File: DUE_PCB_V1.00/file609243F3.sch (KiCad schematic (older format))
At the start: 24 parts, among them J26 Motor_Left2, J37 RPM_Mow, J38 ODO_Left, J39 ODO_Right, J40 Motor_Right, J41 Motor_Left, J42 Cutter, J7 Motor_Right2, U1 MC33926, U2 MC33926

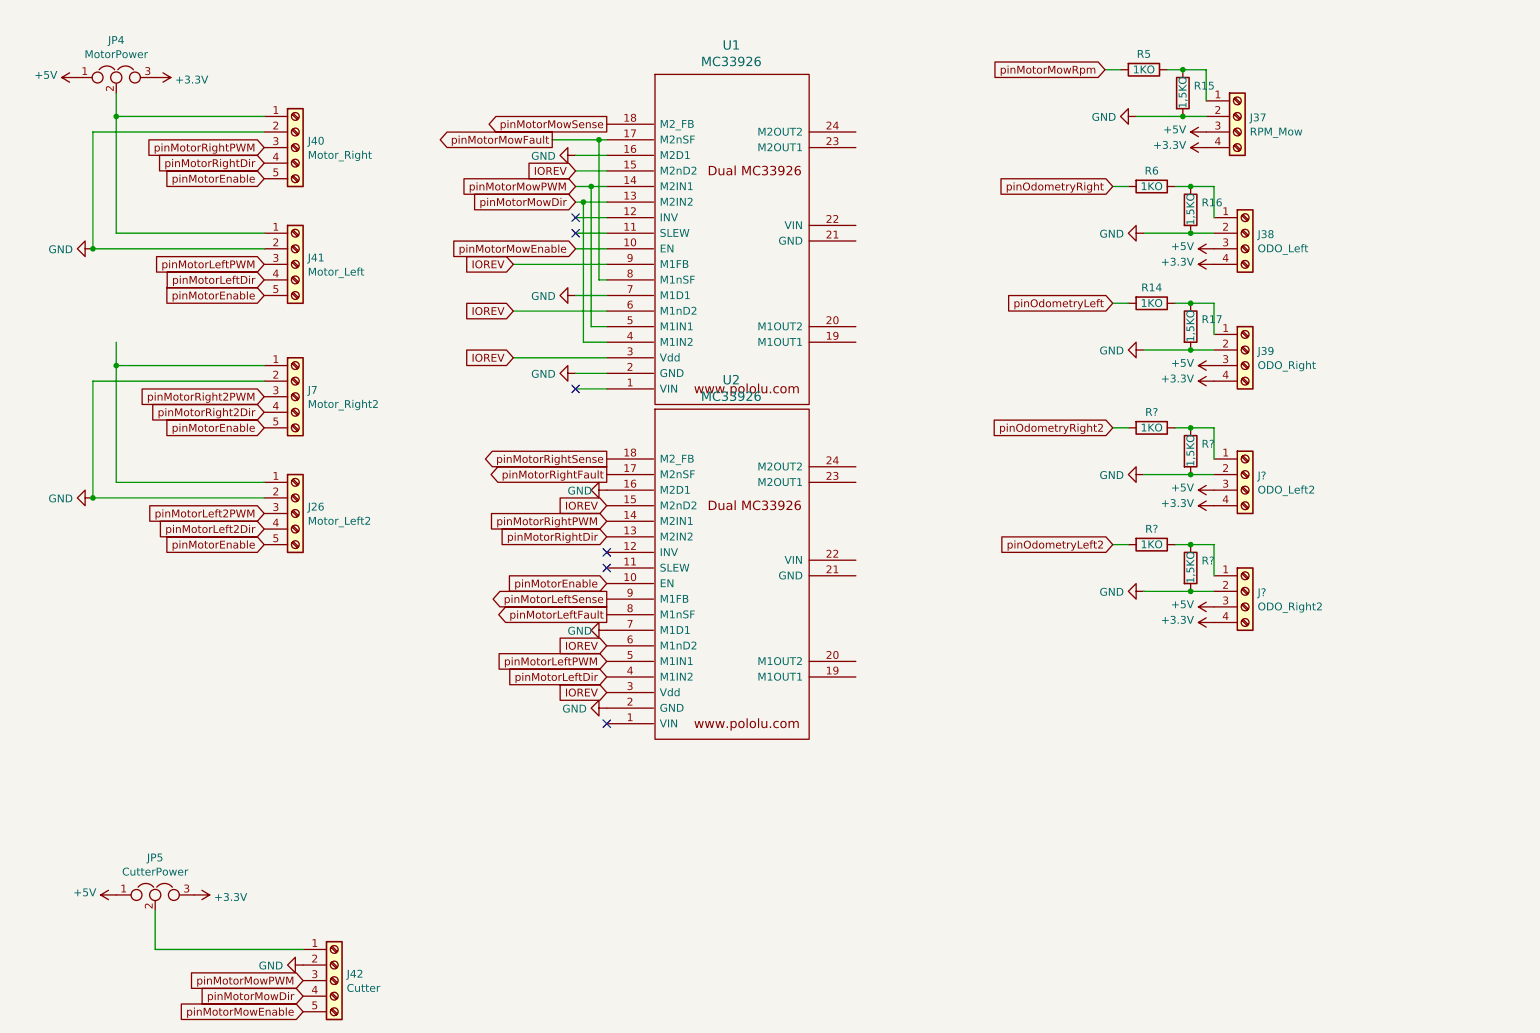
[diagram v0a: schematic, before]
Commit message: New Pins added
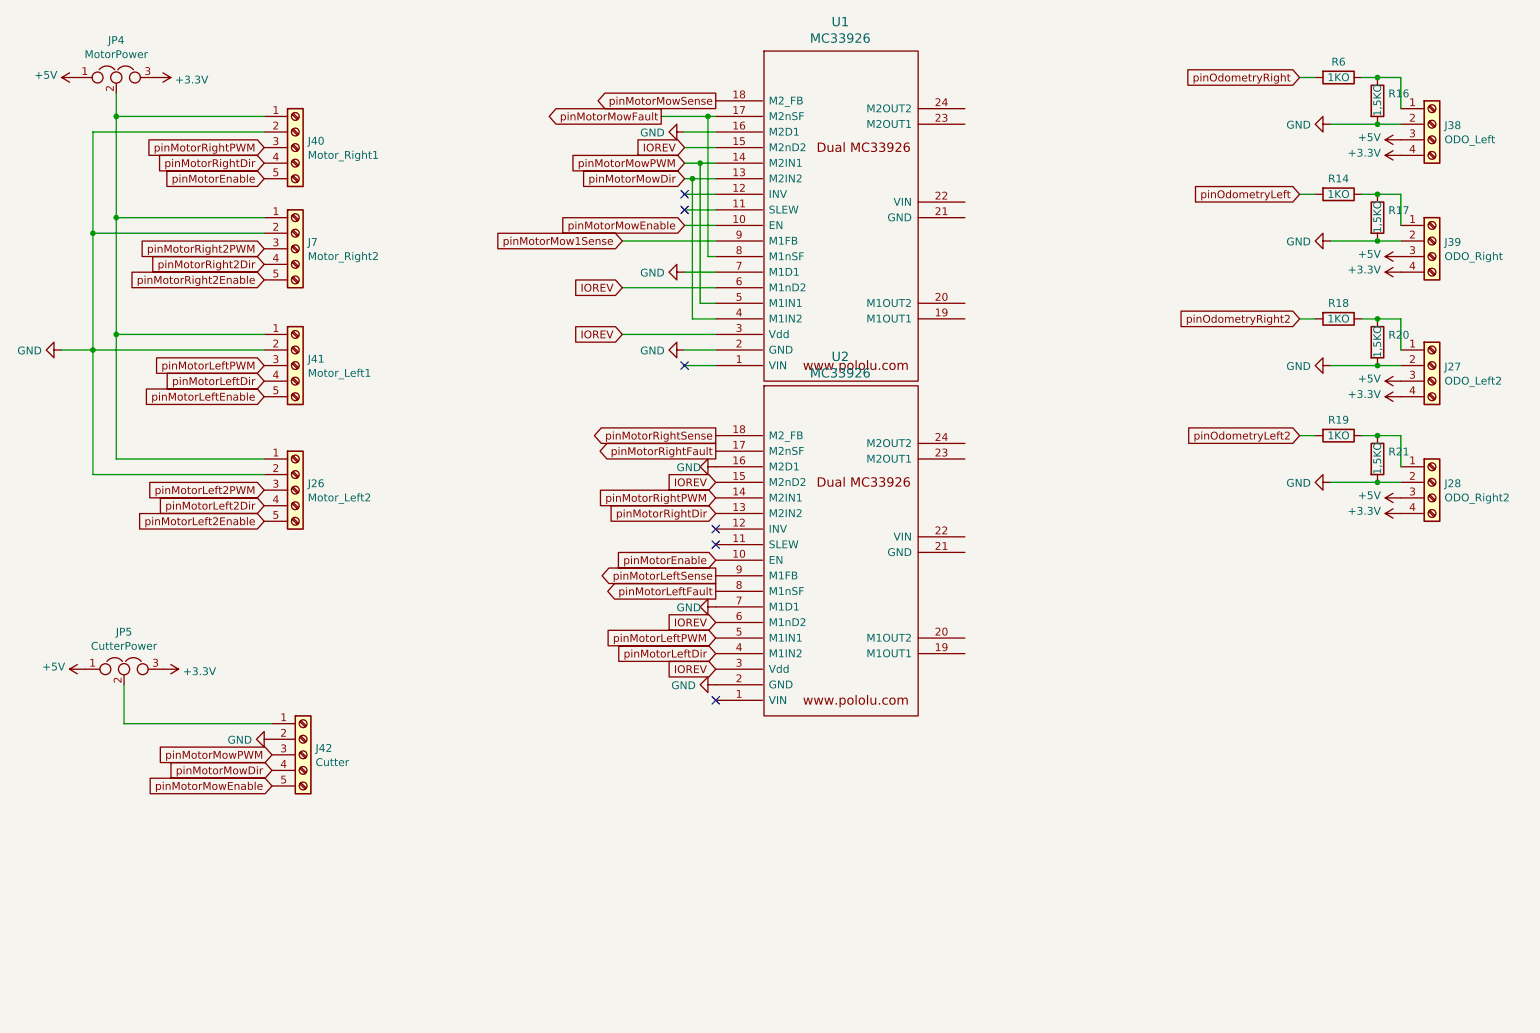
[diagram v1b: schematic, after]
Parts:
- removed J37: RPM_Mow, Connector_PinHeader_2.54mm:PinHeader_1x04_P2.54mm_Vertical, symbol Connector:Screw_Terminal_01x04
- removed R15: 1,5KO, Resistor_THT:R_Axial_DIN0207_L6.3mm_D2.5mm_P2.54mm_Vertical, symbol Device:R
- removed R5: 1KO, Resistor_THT:R_Axial_DIN0207_L6.3mm_D2.5mm_P2.54mm_Vertical, symbol Device:R
- J40: value Motor_Right -> Motor_Right1
- J41: value Motor_Left -> Motor_Left1
- gave numbers to parts that had none: 6
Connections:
- net IOREV: no longer U1.9 (M1FB)
- net pinMotorEnable: no longer J26.5 (Pin_5), J41.5 (Pin_5), J7.5 (Pin_5)
- net at J40.1 (Pin_1), J41.1 (Pin_1), JP4.2: now also J26.1 (Pin_1), J7.1 (Pin_1)
- new net pinMotorLeft2Enable: J26.5 (Pin_5)
- new net pinMotorLeftEnable: J41.5 (Pin_5)
- new net pinMotorMow1Sense: U1.9 (M1FB)
- new net pinMotorRight2Enable: J7.5 (Pin_5)
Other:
- moved on the sheet: J26, J27, J28, J38, J39, J41, J42, J7, JP5, R14, R16, R17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

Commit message: Change to JST-XH
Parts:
- J26, J40, J41, J42, J7: footprint Connector_PinSocket_2.54mm:PinSocket_1x05_P2.54mm_Vertical -> Connector_JST:JST_XH_B5B-XH-A_1x05_P2.50mm_Vertical
- J27, J28, J38, J39: footprint Connector_PinHeader_2.54mm:PinHeader_1x04_P2.54mm_Vertical -> Connector_JST:JST_XH_B4B-XH-A_1x04_P2.50mm_Vertical
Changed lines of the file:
@@
 F 0 "J38" H 9680 1292 50  0000 L CNN
 F 1 "ODO_Left" H 9680 1201 50  0000 L CNN
-F 2 "Connector_PinHeader_2.54mm:PinHeader_1x04_P2.54mm_Vertical" H 9600 1300 50  0001 C CNN
+F 2 "Connector_JST:JST_XH_B4B-XH-A_1x04_P2.50mm_Vertical" H 9600 1300 50  0001 C CNN
 F 3 "~" H 9600 1300 50  0001 C CNN
 	1    9600 1300
@@
 F 0 "J39" H 9680 2042 50  0000 L CNN
 F 1 "ODO_Right" H 9680 1951 50  0000 L CNN
-F 2 "Connector_PinHeader_2.54mm:PinHeader_1x04_P2.54mm_Vertical" H 9600 2050 50  0001 C CNN
+F 2 "Connector_JST:JST_XH_B4B-XH-A_1x04_P2.50mm_Vertical" H 9600 2050 50  0001 C CNN
 F 3 "~" H 9600 2050 50  0001 C CNN
 	1    9600 2050
@@
 F 0 "J40" H 2380 1492 50  0000 L CNN
 F 1 "Motor_Right1" H 2380 1401 50  0000 L CNN
-F 2 "Connector_PinSocket_2.54mm:PinSocket_1x05_P2.54mm_Vertical" H 2300 1450 50  0001 C CNN
+F 2 "Connector_JST:JST_XH_B5B-XH-A_1x05_P2.50mm_Vertical" H 2300 1450 50  0001 C CNN
 F 3 "~" H 2300 1450 50  0001 C CNN
 	1    2300 1450
@@
 F 0 "J41" H 2380 2892 50  0000 L CNN
 F 1 "Motor_Left1" H 2380 2801 50  0000 L CNN
-F 2 "Connector_PinSocket_2.54mm:PinSocket_1x05_P2.54mm_Vertical" H 2300 2850 50  0001 C CNN
+F 2 "Connector_JST:JST_XH_B5B-XH-A_1x05_P2.50mm_Vertical" H 2300 2850 50  0001 C CNN
 F 3 "~" H 2300 2850 50  0001 C CNN
 	1    2300 2850
@@
 F 0 "J42" H 2430 5392 50  0000 L CNN
 F 1 "Cutter" H 2430 5301 50  0000 L CNN
-F 2 "Connector_PinSocket_2.54mm:PinSocket_1x05_P2.54mm_Vertical" H 2350 5350 50  0001 C CNN
+F 2 "Connector_JST:JST_XH_B5B-XH-A_1x05_P2.50mm_Vertical" H 2350 5350 50  0001 C CNN
 F 3 "~" H 2350 5350 50  0001 C CNN
 	1    2350 5350
@@
 F 0 "J7" H 2380 2142 50  0000 L CNN
 F 1 "Motor_Right2" H 2380 2051 50  0000 L CNN
-F 2 "Connector_PinSocket_2.54mm:PinSocket_1x05_P2.54mm_Vertical" H 2300 2100 50  0001 C CNN
+F 2 "Connector_JST:JST_XH_B5B-XH-A_1x05_P2.50mm_Vertical" H 2300 2100 50  0001 C CNN
 F 3 "~" H 2300 2100 50  0001 C CNN
 	1    2300 2100
@@
 F 0 "J26" H 2380 3692 50  0000 L CNN
 F 1 "Motor_Left2" H 2380 3601 50  0000 L CNN
-F 2 "Connector_PinSocket_2.54mm:PinSocket_1x05_P2.54mm_Vertical" H 2300 3650 50  0001 C CNN
+F 2 "Connector_JST:JST_XH_B5B-XH-A_1x05_P2.50mm_Vertical" H 2300 3650 50  0001 C CNN
 F 3 "~" H 2300 3650 50  0001 C CNN
 	1    2300 3650
@@
 F 0 "J27" H 9680 2842 50  0000 L CNN
 F 1 "ODO_Left2" H 9680 2751 50  0000 L CNN
-F 2 "Connector_PinHeader_2.54mm:PinHeader_1x04_P2.54mm_Vertical" H 9600 2850 50  0001 C CNN
+F 2 "Connector_JST:JST_XH_B4B-XH-A_1x04_P2.50mm_Vertical" H 9600 2850 50  0001 C CNN
 F 3 "~" H 9600 2850 50  0001 C CNN
 	1    9600 2850
@@
 F 0 "J28" H 9680 3592 50  0000 L CNN
 F 1 "ODO_Right2" H 9680 3501 50  0000 L CNN
-F 2 "Connector_PinHeader_2.54mm:PinHeader_1x04_P2.54mm_Vertical" H 9600 3600 50  0001 C CNN
+F 2 "Connector_JST:JST_XH_B4B-XH-A_1x04_P2.50mm_Vertical" H 9600 3600 50  0001 C CNN
 F 3 "~" H 9600 3600 50  0001 C CNN
 	1    9600 3600

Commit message: PCB ODO Names Changes
Change ODO LEFT to Right. Create new Schematic PDF. Create New Gerber Files.
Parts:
- J27: value ODO_Left2 -> ODO_Right2
- J28: value ODO_Right2 -> ODO_Left2
- J38: value ODO_Left -> ODO_Right
- J39: value ODO_Right -> ODO_Left
- U1, U2: symbol Lötpad_2,5mm:MC33926 -> Ardumower-rescue:MC33926-Lötpad_2,5mm
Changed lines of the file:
@@
 pinMotorRightPWM
 $Comp
-L Lötpad_2,5mm:MC33926 U?
+L Ardumower-rescue:MC33926-Lötpad_2,5mm U?
 U 1 1 60958C90
 P 5850 4250
@@
 P 9600 1300
 F 0 "J38" H 9680 1292 50  0000 L CNN
-F 1 "ODO_Left" H 9680 1201 50  0000 L CNN
+F 1 "ODO_Right" H 9680 1201 50  0000 L CNN
 F 2 "Connector_JST:JST_XH_B4B-XH-A_1x04_P2.50mm_Vertical" H 9600 1300 50  0001 C CNN
 F 3 "~" H 9600 1300 50  0001 C CNN
@@
 P 9600 2050
 F 0 "J39" H 9680 2042 50  0000 L CNN
-F 1 "ODO_Right" H 9680 1951 50  0000 L CNN
+F 1 "ODO_Left" H 9680 1951 50  0000 L CNN
 F 2 "Connector_JST:JST_XH_B4B-XH-A_1x04_P2.50mm_Vertical" H 9600 2050 50  0001 C CNN
 F 3 "~" H 9600 2050 50  0001 C CNN
@@
 	2100 1350 1000 1350
 $Comp
-L Lötpad_2,5mm:MC33926 U?
+L Ardumower-rescue:MC33926-Lötpad_2,5mm U?
 U 1 1 60958C96
 P 5850 2100
@@
 P 9600 2850
 F 0 "J27" H 9680 2842 50  0000 L CNN
-F 1 "ODO_Left2" H 9680 2751 50  0000 L CNN
+F 1 "ODO_Right2" H 9680 2751 50  0000 L CNN
 F 2 "Connector_JST:JST_XH_B4B-XH-A_1x04_P2.50mm_Vertical" H 9600 2850 50  0001 C CNN
 F 3 "~" H 9600 2850 50  0001 C CNN
@@
 P 9600 3600
 F 0 "J28" H 9680 3592 50  0000 L CNN
-F 1 "ODO_Right2" H 9680 3501 50  0000 L CNN
+F 1 "ODO_Left2" H 9680 3501 50  0000 L CNN
 F 2 "Connector_JST:JST_XH_B4B-XH-A_1x04_P2.50mm_Vertical" H 9600 3600 50  0001 C CNN
 F 3 "~" H 9600 3600 50  0001 C CNN
